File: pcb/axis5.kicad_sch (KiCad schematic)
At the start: 7 parts, among them J15 Mini v1.0 / 15-hole socket, J25 MOTOR PHASES male 1x3, J35 ENCODER breakout FEMALE 1x6

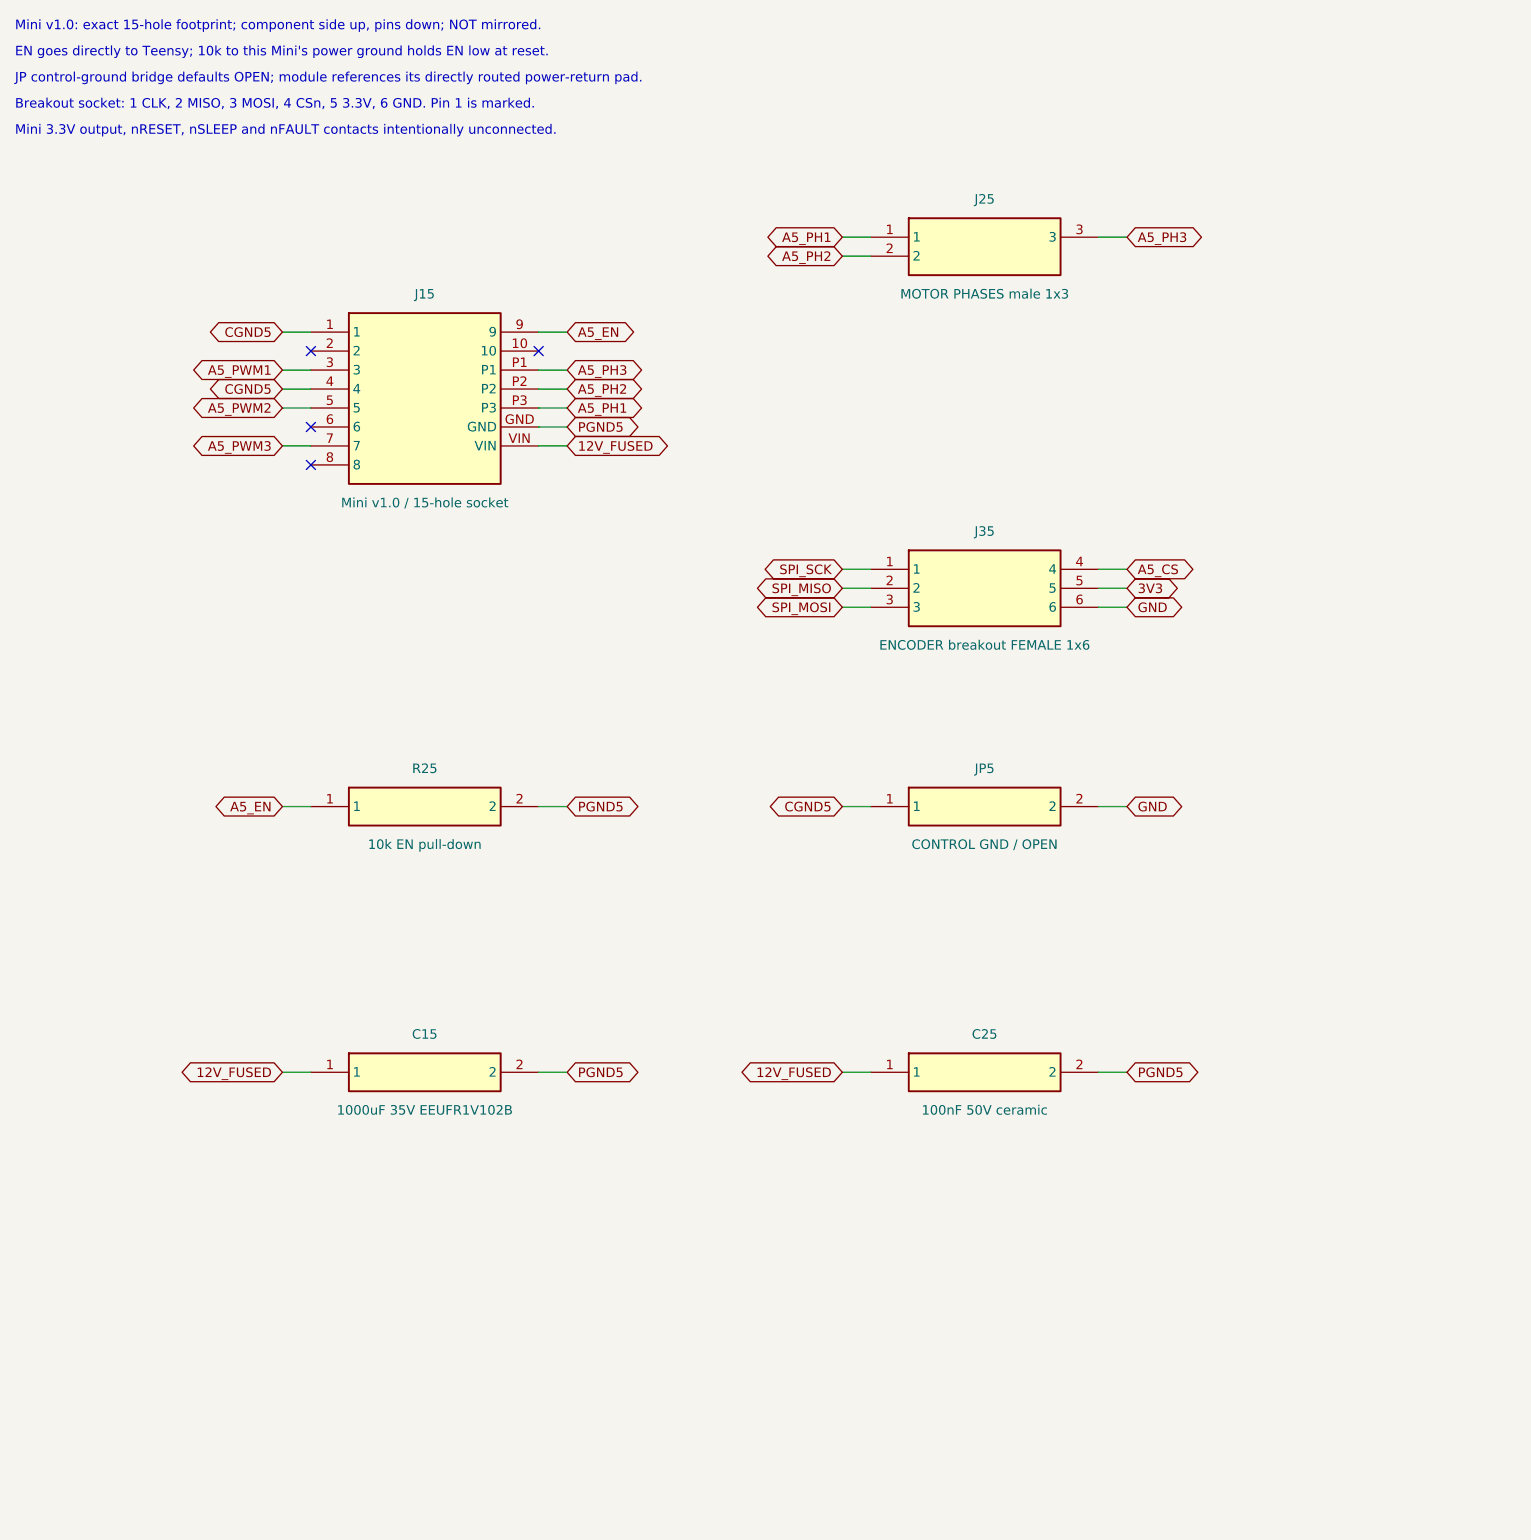
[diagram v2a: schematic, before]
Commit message: feat: relayout carrier with edge connectors and hardware kill
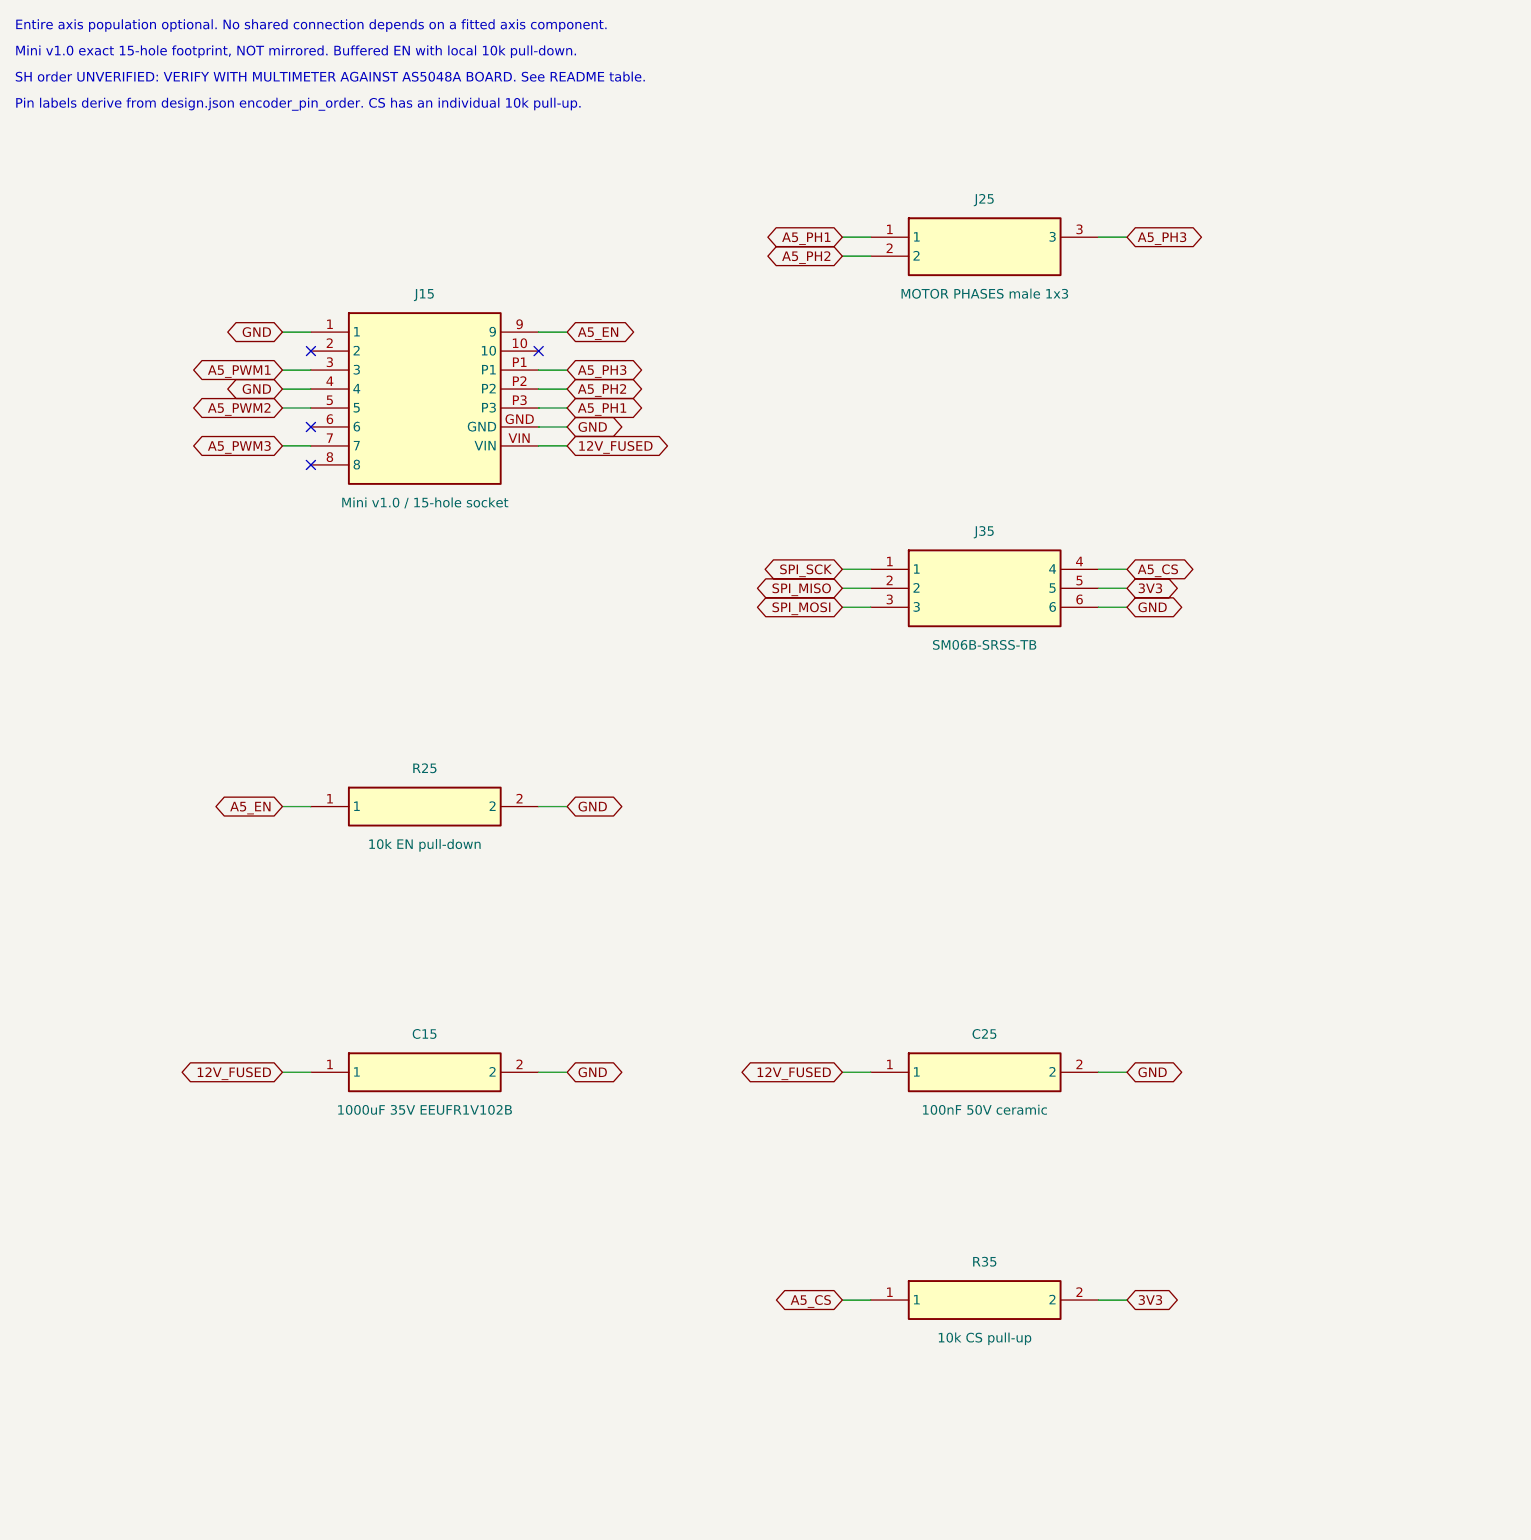
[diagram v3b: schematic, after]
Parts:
- removed JP5: CONTROL GND / OPEN, TrueSkate:GroundBridge_THT, symbol TrueSkate:JP5
- added R35: 10k CS pull-up, TrueSkate:Edge_R_Axial_DIN0207_L6.3mm_D2.5mm_P7.62mm_Horizontal, symbol TrueSkate:R35
- C15: footprint Capacitor_THT:CP_Radial_D12.5mm_P5.00mm -> TrueSkate:Edge_CP_Radial_D12.5mm_P5.00mm
- C25: footprint Capacitor_THT:C_Disc_D5.0mm_W2.5mm_P5.00mm -> TrueSkate:Edge_C_Disc_D5.0mm_W2.5mm_P5.00mm
- J25: footprint Connector_PinHeader_2.54mm:PinHeader_1x03_P2.54mm_Vertical -> TrueSkate:Edge_PinHeader_1x03_P2.54mm_Vertical
- J35: value ENCODER breakout FEMALE 1x6 -> SM06B-SRSS-TB; footprint Connector_PinSocket_2.54mm:PinSocket_1x06_P2.54mm_Vertical -> TrueSkate:Edge_JST_SH_SM06B-SRSS-TB_1x06-1MP_P1.00mm_Horizontal
- R25: footprint Resistor_THT:R_Axial_DIN0207_L6.3mm_D2.5mm_P7.62mm_Horizontal -> TrueSkate:Edge_R_Axial_DIN0207_L6.3mm_D2.5mm_P7.62mm_Horizontal
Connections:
- net CGND5 is gone; now on net GND: J15.1, J15.4
- net PGND5 is gone; now on net GND: C15.2, C25.2, J15.GND, R25.2
- net 3V3: now also R35.2
- net A5_CS: now also R35.1
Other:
- note added: "Entire axis population optional. No shared connection depends on a fitted axis component."
- note added: "Mini v1.0 exact 15-hole footprint, NOT mirrored. Buffered EN with local 10k pull-down."
- note added: "Pin labels derive from design.json encoder_pin_order. CS has an individual 10k pull-up."
- note added: "SH order UNVERIFIED: VERIFY WITH MULTIMETER AGAINST AS5048A BOARD. See README table."
- note removed: "Breakout socket: 1 CLK, 2 MISO, 3 MOSI, 4 CSn, 5 3.3V, 6 GND. Pin 1 is marked."
- note removed: "EN goes directly to Teensy; 10k to this Mini's power ground holds EN low at reset."
- note removed: "JP control-ground bridge defaults OPEN; module references its directly routed power-return pad."
- note removed: "Mini 3.3V output, nRESET, nSLEEP and nFAULT contacts intentionally unconnected."
- note removed: "Mini v1.0: exact 15-hole footprint; component side up, pins down; NOT mirrored."
